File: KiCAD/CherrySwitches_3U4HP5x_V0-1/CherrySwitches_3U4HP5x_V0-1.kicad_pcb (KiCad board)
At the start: 2 copper layers, 20.3 x 128.5 mm, 8 parts, among them J1 Conn_02x05_Odd_Even, SW1 SW_SPST, SW2 SW_SPST, SW3 SW_SPST, SW4 SW_SPST, SW5 SW_SPST

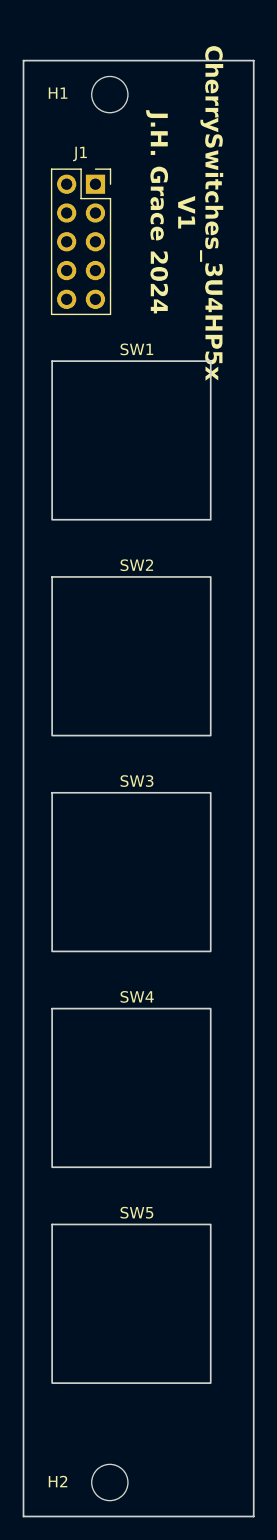
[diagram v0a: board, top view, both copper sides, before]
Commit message: updated PCB widths to better conform to Eurorack standards
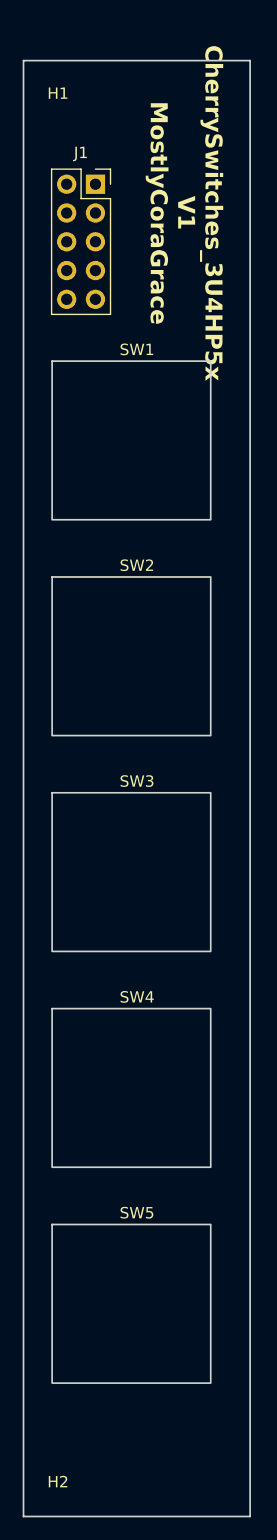
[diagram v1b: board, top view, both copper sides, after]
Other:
- board size 20.3 x 128.5 mm -> 20 x 128.5 mm
- board text added: "CherrySwitches_3U4HP5x V1 MostlyCoraGrace"
- board text removed: "CherrySwitches_3U4HP5x V1 J.H. Grace 2024"
